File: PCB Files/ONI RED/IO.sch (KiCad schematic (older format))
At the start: 1 part, among them U10 LFE5UM-25F-6BG381C

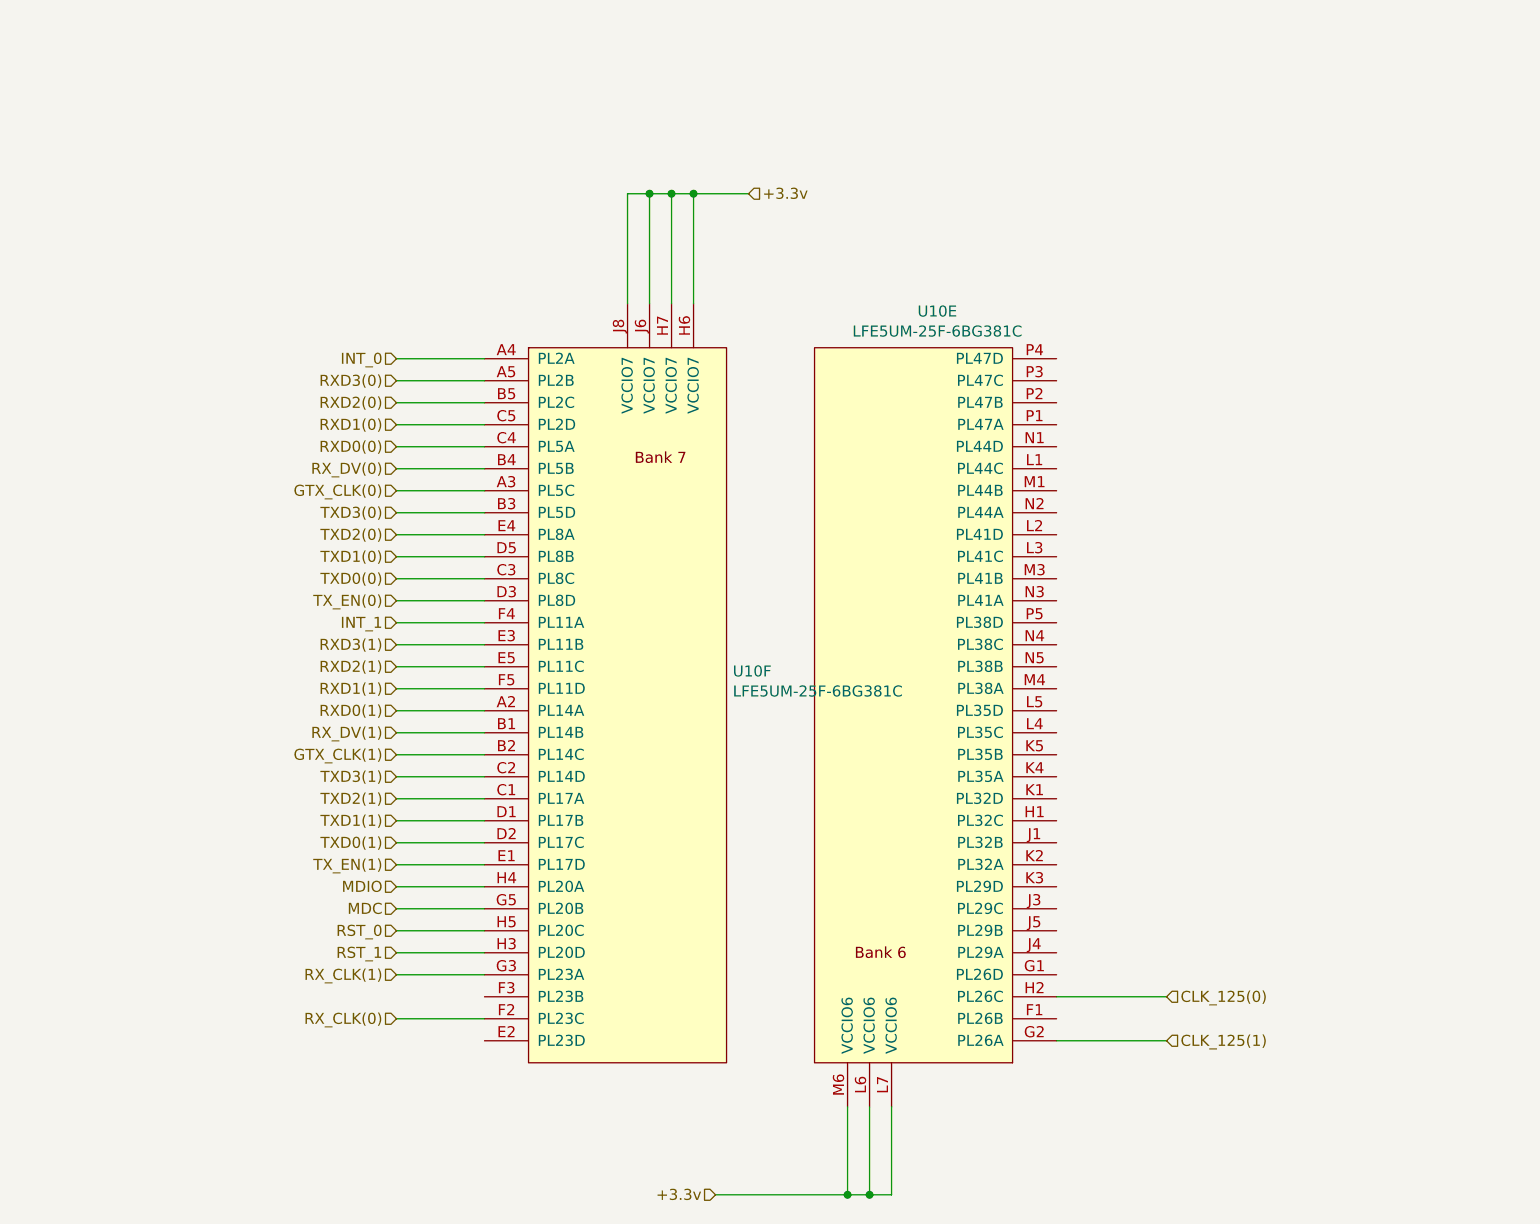
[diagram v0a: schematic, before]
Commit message: Added extra PHYs and expanded IO
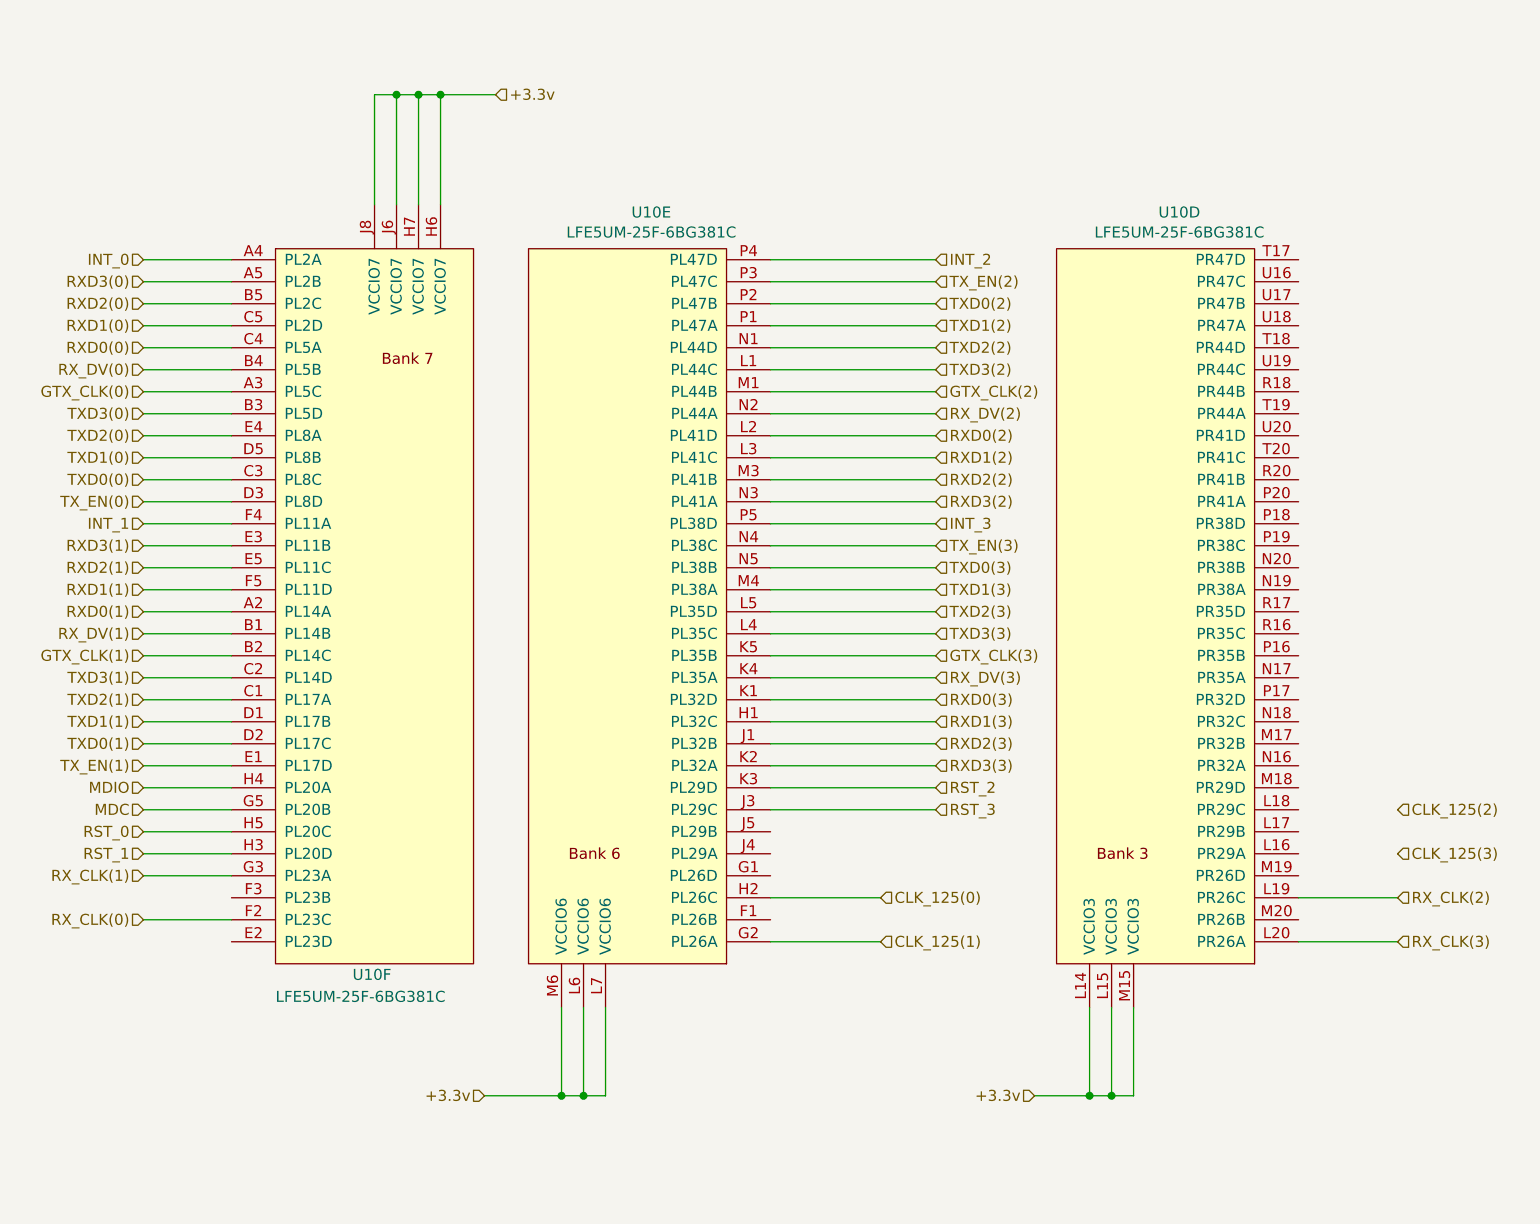
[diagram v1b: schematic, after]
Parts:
- added unit 4 of U10
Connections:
- net +3.3v: now also U10.L14 (VCCIO3), U10.L15 (VCCIO3), U10.M15 (VCCIO3)
- net RXD1(3): now reaches U10.H1 (PL32C)
- net RXD2(3): now reaches U10.J1 (PL32B)
- net RST_3: now reaches U10.J3 (PL29C)
- net RXD0(3): now reaches U10.K1 (PL32D)
- net RXD3(3): now reaches U10.K2 (PL32A)
- net RST_2: now reaches U10.K3 (PL29D)
- net RX_DV(3): now reaches U10.K4 (PL35A)
- net GTX_CLK(3): now reaches U10.K5 (PL35B)
- net TXD3(2): now reaches U10.L1 (PL44C)
- net RXD0(2): now reaches U10.L2 (PL41D)
- net RXD1(2): now reaches U10.L3 (PL41C)
- net TXD3(3): now reaches U10.L4 (PL35C)
- net TXD2(3): now reaches U10.L5 (PL35D)
- net GTX_CLK(2): now reaches U10.M1 (PL44B)
- net RXD2(2): now reaches U10.M3 (PL41B)
- net TXD1(3): now reaches U10.M4 (PL38A)
- net TXD2(2): now reaches U10.N1 (PL44D)
- net RX_DV(2): now reaches U10.N2 (PL44A)
- net RXD3(2): now reaches U10.N3 (PL41A)
- net TX_EN(3): now reaches U10.N4 (PL38C)
- net TXD0(3): now reaches U10.N5 (PL38B)
- net TXD1(2): now reaches U10.P1 (PL47A)
- net TXD0(2): now reaches U10.P2 (PL47B)
- net TX_EN(2): now reaches U10.P3 (PL47C)
- net INT_2: now reaches U10.P4 (PL47D)
- net INT_3: now reaches U10.P5 (PL38D)
- new net RX_CLK(2): U10.L19 (PR26C)
- new net RX_CLK(3): U10.L20 (PR26A)
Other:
- moved on the sheet: U10E, U10F

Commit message: Continued routing IO and begun implementing DDR2 RAM
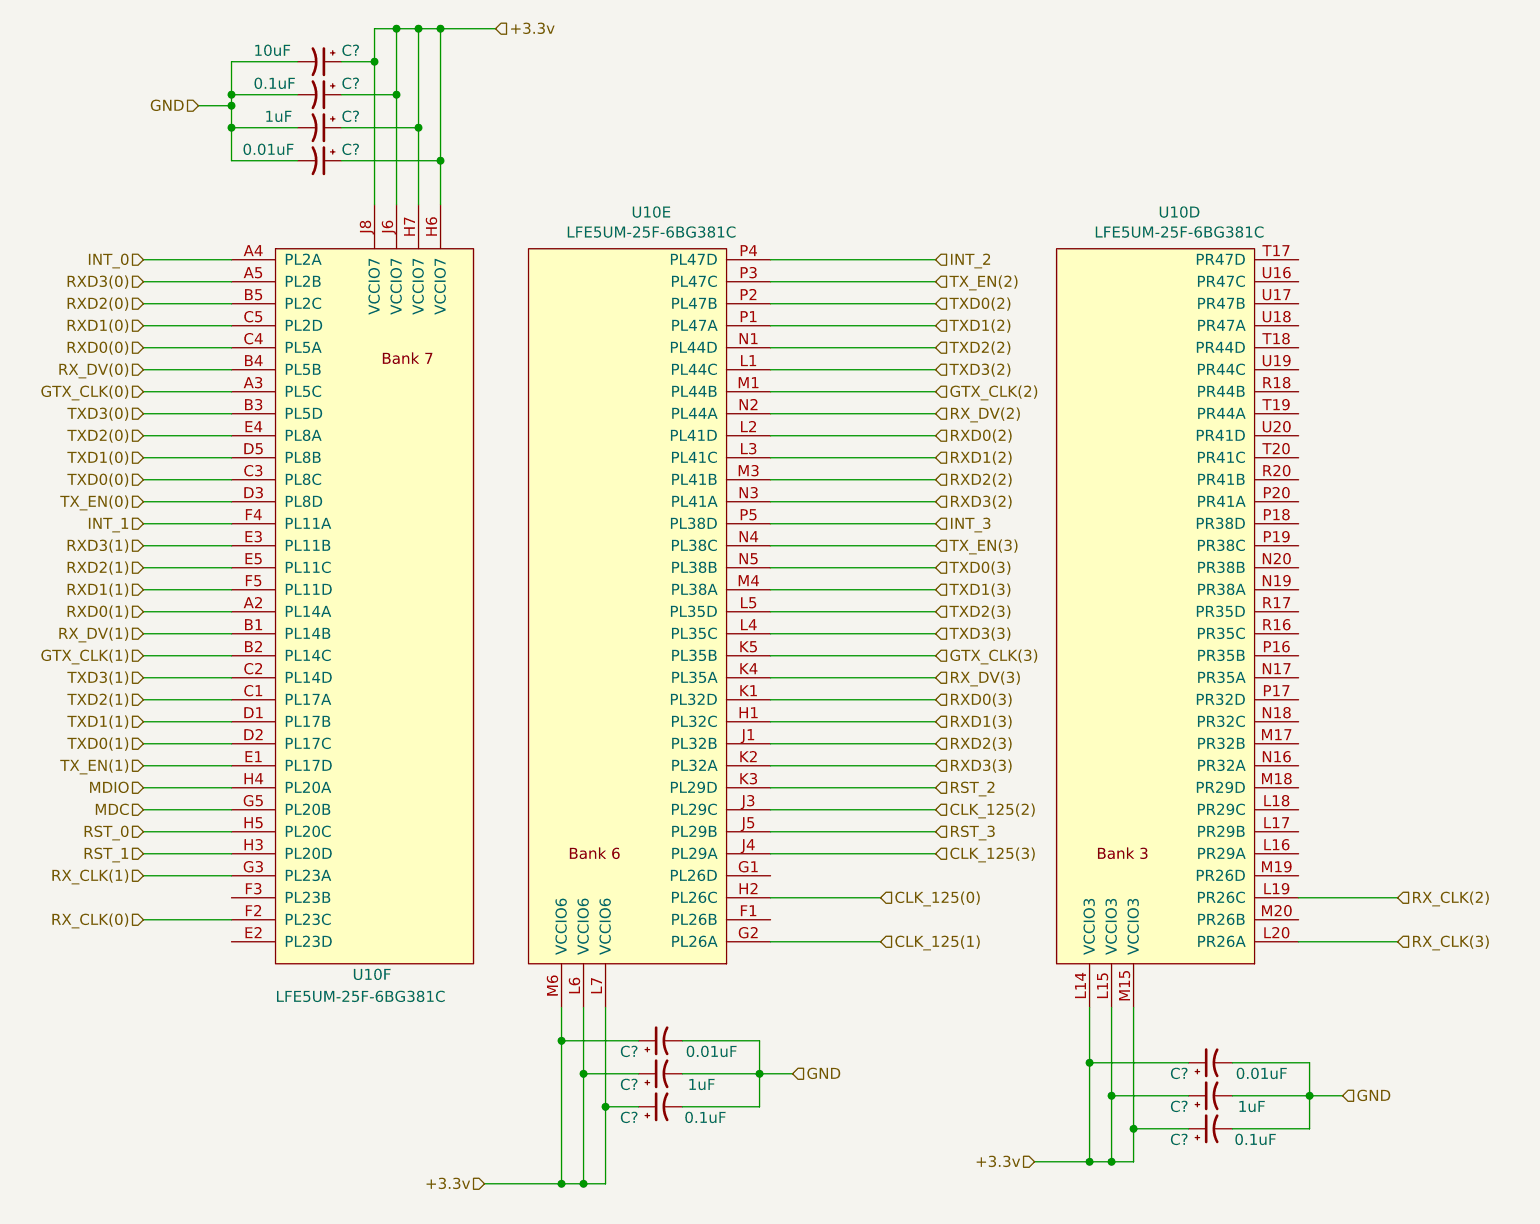
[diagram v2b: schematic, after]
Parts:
- added C?: 10uF, symbol Device:CP1_Small
- added C? (x3): 0.1uF, symbol Device:CP1_Small
- added C? (x3): 1uF, symbol Device:CP1_Small
- added C? (x3): 0.01uF, symbol Device:CP1_Small
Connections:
- net +3.3v: now also C?.1, C?.1, C?.1, C?.1, C?.1, C?.1, C?.1, C?.1, C?.1, C?.1
- net CLK_125(2): now also U10.J3 (PL29C)
- net CLK_125(3): now also U10.J4 (PL29A)
- net RST_3: now also U10.J5 (PL29B); no longer U10.J3 (PL29C)
- new net GND: C?.2, C?.2, C?.2, C?.2, C?.2, C?.2, C?.2, C?.2, C?.2, C?.2
